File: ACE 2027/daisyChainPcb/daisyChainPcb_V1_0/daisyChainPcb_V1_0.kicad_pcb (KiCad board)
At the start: 2 copper layers, 56.5 x 97 mm, 26 parts, among them J201 Pads, J202 XT30, J203 XT30, J204 Pads, J205 Pads, J206 RJ45, J207 RJ45, U101 AP7361C-33E-13

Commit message: Ready for PCB PR
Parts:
- moved TP201 60.9 mm to (162.9, 95.8)
- moved TP203 57.1 mm to (158.9, 95.8)
- moved TP205 51.0 mm to (152.8, 78.6)
- moved TP208 45.9 mm to (141.7, 46.8)
- moved TP206 42.9 mm to (163.0, 113.4)
- moved TP207 40.4 mm to (153.0, 84.0)
- moved TP211 35.5 mm to (157.8, 61.3)
- moved TP202 31.0 mm to (152.8, 73.1)
- moved TP204 28.7 mm to (147.5, 73.0)
- moved TP209 27.6 mm to (141.2, 117.6)
- moved TP210 11.3 mm to (135.8, 115.9)
- moved R202 2.57 mm to (151.0, 63.2)
- moved R201 2.57 mm to (153.0, 63.2)
- moved J201 1.16 mm to (162.2, 81.3)
- moved J205 1.16 mm to (156.3, 86.9)
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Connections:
- J201 pad 2: /Controle/48V -> +48V
- J202 pad 2: /Controle/48V -> +48V
- J203 pad 2: /Controle/48V -> +48V
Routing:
- net +48V: track 0.00 -> 98.9 mm, vias 0 -> 1
- net /Controle/SCL: track 0.00 -> 92.4 mm, vias 0 -> 1
- net /Controle/SDA: track 0.00 -> 92.1 mm, vias 0 -> 1
- net +5V: track 0.00 -> 85.0 mm, vias 0 -> 3
- net /Controle/TX: track 0.00 -> 80.7 mm, vias 0 -> 3
- net /Controle/CAN_N: track 0.00 -> 80.4 mm, vias 0 -> 1
- net /Controle/CAN_P: track 0.00 -> 80.4 mm, vias 0 -> 1
- net /Controle/RX: track 0.00 -> 79.6 mm, vias 0 -> 3
- net VCC_3V3: track 0.00 -> 10.8 mm
- net power_GND: track 0.00 -> 7.65 mm
- added copper zone on B.Cu, net power_GND
- added copper zone on F.Cu, net signal_GND
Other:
- board text added: "3.3V"
- board text added: "5V"
- board text added: "SCL"
- board text added: "SDA"
- board text added: "Signal GND"

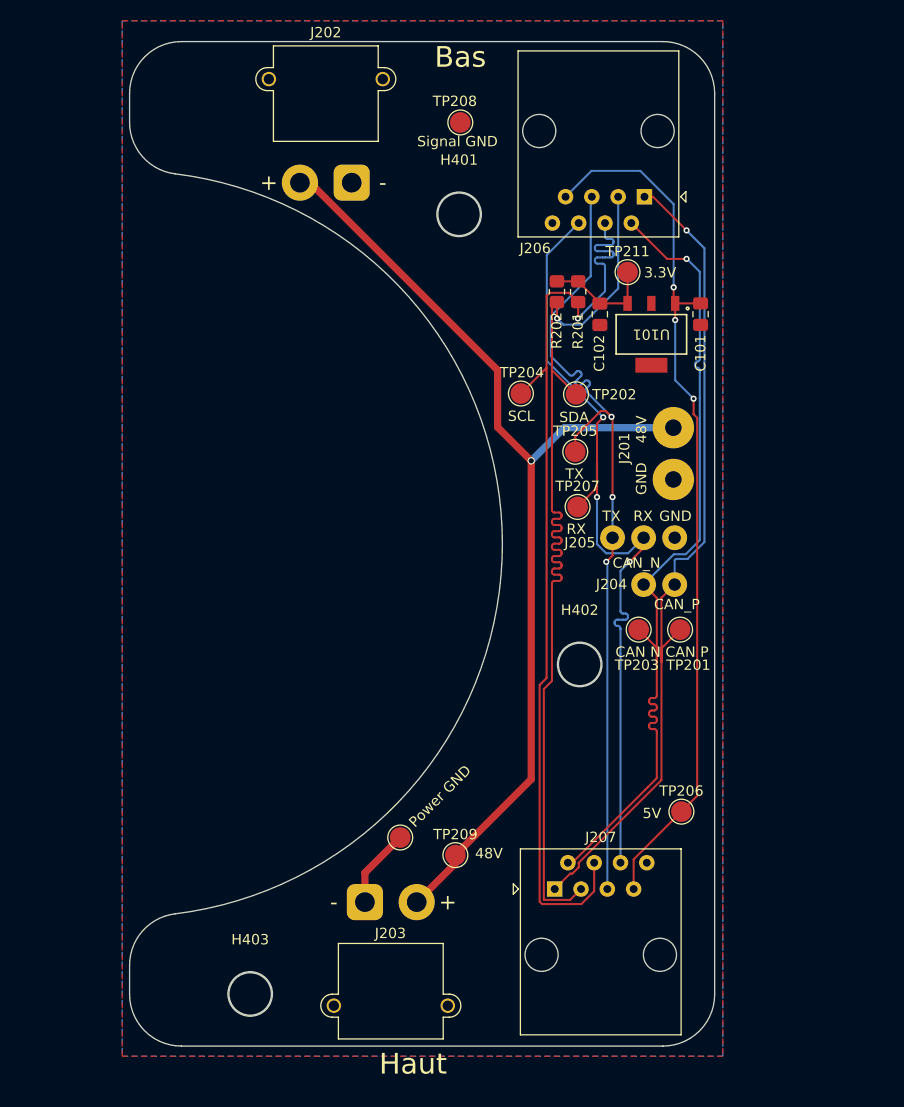
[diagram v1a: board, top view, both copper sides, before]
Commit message: amélioration de la forme du pcb
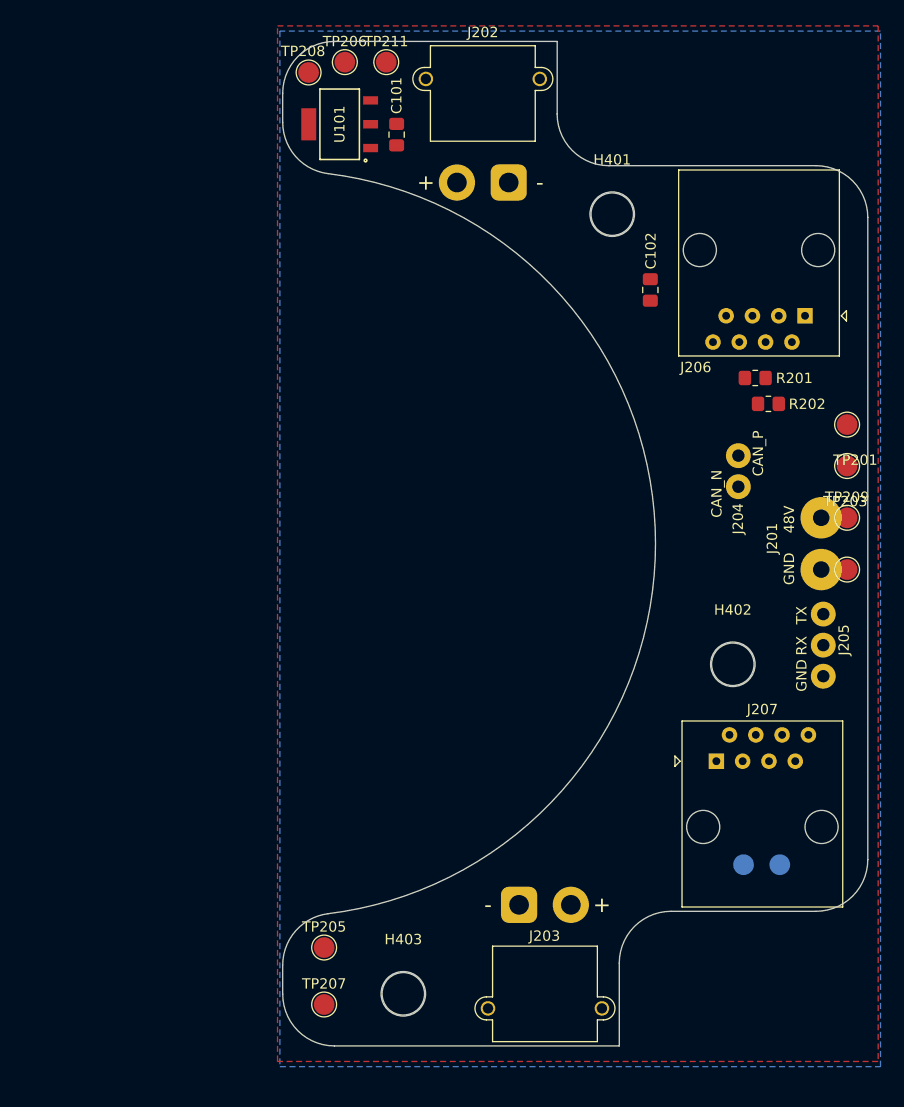
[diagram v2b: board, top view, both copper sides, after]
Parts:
- TP202, TP204: moved to B.Cu
- moved TP206 79.3 mm to (130.5, 41.0)
- moved TP207 53.9 mm to (128.5, 132.0)
- moved TP205 53.7 mm to (128.5, 126.5)
- moved TP204 51.9 mm to (172.5, 118.5), turned to 180 degrees
- moved TP210 50.3 mm to (179.0, 90.0)
- moved TP209 49.9 mm to (179.0, 85.0)
- moved TP202 48.2 mm to (169.0, 118.5), turned to 180 degrees
- moved U101 36.3 mm to (130.0, 47.0), turned to 90 degrees
- moved C101 34.1 mm to (135.5, 48.0), turned to 90 degrees
- moved TP211 30.9 mm to (134.5, 41.0)
- moved TP203 25.6 mm to (179.0, 80.0)
- moved TP201 25.5 mm to (179.0, 76.0)
- moved J205 24.4 mm to (176.7, 100.3), turned to 90 degrees
- moved R202 23.1 mm to (171.4, 74.0), turned to 180 degrees
- moved J207 19.9 mm to (166.4, 108.5)
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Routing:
- net +48V: track 98.9 -> 0.00 mm, vias 1 -> 0
- net /Controle/SCL: track 92.4 -> 0.00 mm, vias 1 -> 0
- net /Controle/SDA: track 92.1 -> 0.00 mm, vias 1 -> 0
- net +5V: track 85.0 -> 0.00 mm, vias 3 -> 0
- net /Controle/TX: track 80.7 -> 0.00 mm, vias 3 -> 0
- net /Controle/CAN_N: track 80.4 -> 0.00 mm, vias 1 -> 0
- net /Controle/CAN_P: track 80.4 -> 0.00 mm, vias 1 -> 0
- net /Controle/RX: track 79.6 -> 0.00 mm, vias 3 -> 0
- net VCC_3V3: track 10.8 -> 0.00 mm
- net power_GND: track 7.65 -> 0.00 mm
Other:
- outline, holes or cut-outs redrawn
- board text removed: "3.3V"
- board text removed: "48V"
- board text removed: "5V"
- board text removed: "Bas"
- board text removed: "CAN N"
- board text removed: "CAN P"
- board text removed: "Haut"
- board text removed: "Power GND"
- board text removed: "RX"
- board text removed: "SCL"
- board text removed: "SDA"
- board text removed: "Signal GND"
- board text removed: "TX"

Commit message: Version optimisé du PCB
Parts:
- TP201, TP203, TP205, TP207: moved to B.Cu
- TP202, TP204: moved to F.Cu
- moved TP207 45.1 mm to (172.0, 120.0), turned to 180 degrees
- moved TP204 44.8 mm to (128.5, 127.0), turned to 0 degrees
- moved TP202 43.2 mm to (128.0, 132.0), turned to 0 degrees
- moved TP205 39.0 mm to (167.0, 120.0), turned to 180 degrees
- moved TP203 26.7 mm to (173.0, 54.0), turned to 180 degrees
- moved TP201 22.1 mm to (177.5, 54.0), turned to 180 degrees
- moved J207 4.00 mm to (162.4, 108.5)
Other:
- outline, holes or cut-outs redrawn

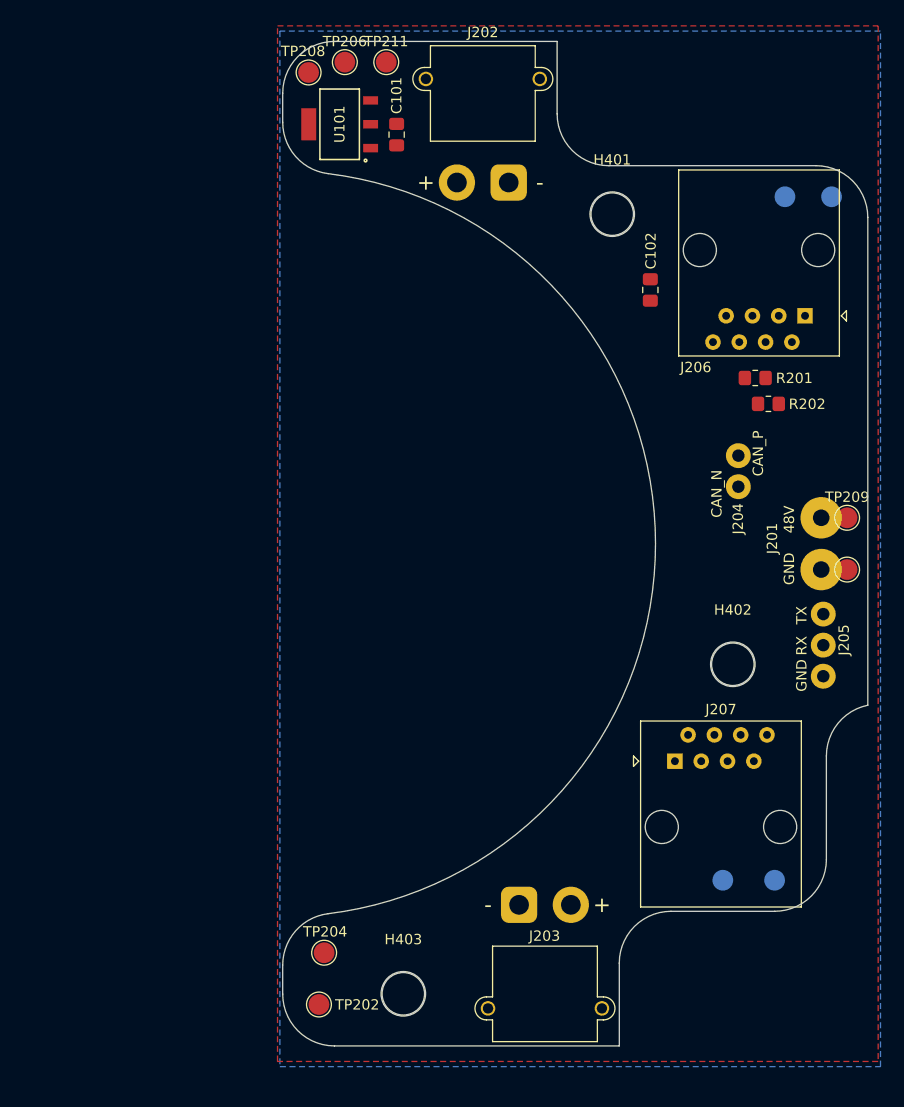
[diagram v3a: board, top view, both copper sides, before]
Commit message: deplacement petit capaciteur
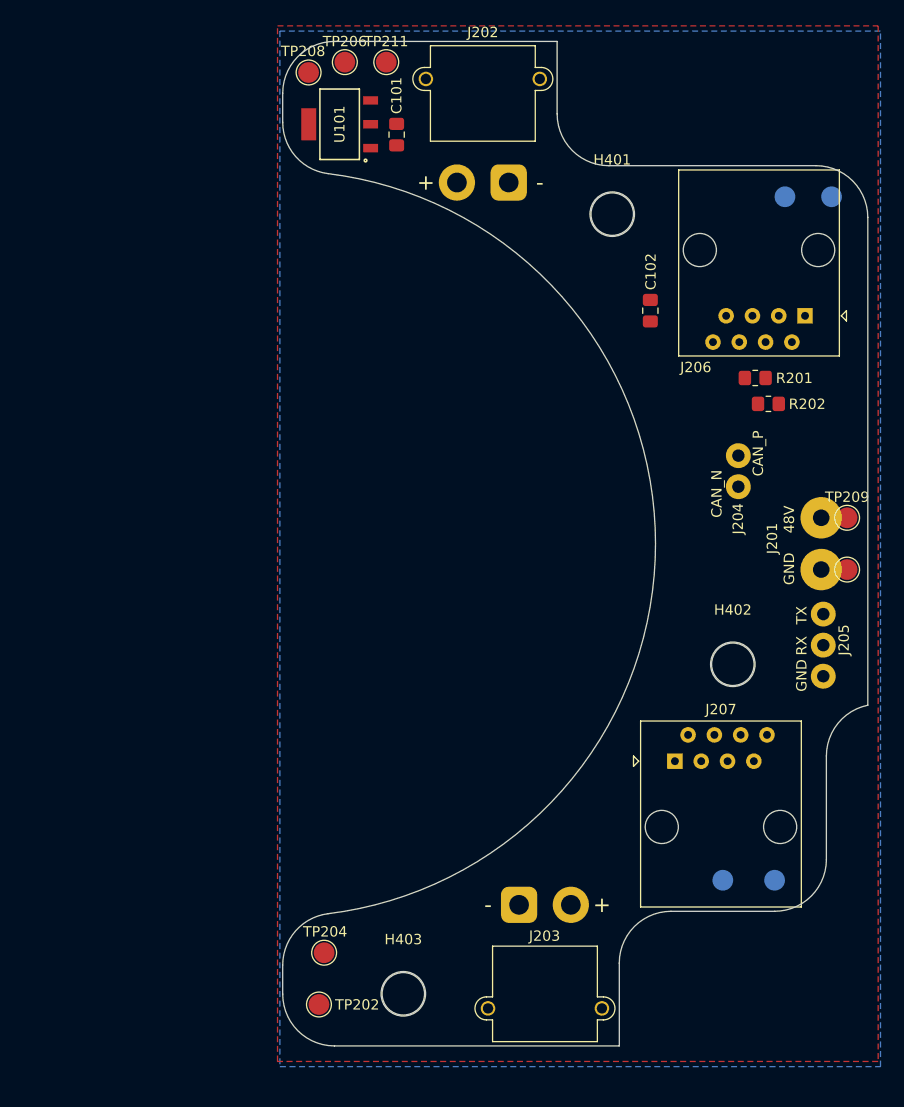
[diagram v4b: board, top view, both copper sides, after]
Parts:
- moved C102 2.00 mm to (160.0, 65.0)
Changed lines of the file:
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@@
 	(footprint "Capacitor_SMD:C_0805_2012Metric_Pad1.18x1.45mm_HandSolder"
 		(layer "F.Cu")
-		(at 160 63 90)
+		(at 160 65 90)
 		(descr "Capacitor SMD 0805 (2012 Metric), square (rectangular) end terminal, IPC-7351 nominal with elongated pad for handsoldering. (Body size source: IPC-SM-782 page 76, https://www.pcb-3d.com/wordpress/wp-content/uploads/ipc-sm-782a_amendment_1_and_2.pdf, https://docs.google.com/spreadsheets/d/1BsfQQcO9C6DZCsRaXUlFlo91Tg2WpOkGARC1WS5S8t0/edit?usp=sharing)")
 		(tags "capacitor handsolder")
@@
 		(end 124.5 46.80602)
 		(stroke
-			(width 0)
+			(width 0.1)
 			(type default)
 		)
@@
 		(end 129.5 39)
 		(stroke
-			(width 0)
+			(width 0.1)
 			(type default)
 		)
@@
 		(end 124.5 131)
 		(stroke
-			(width 0)
+			(width 0.1)
 			(type default)
 		)
@@
 		(end 128.890244 123.231299)
 		(stroke
-			(width 0)
+			(width 0.1)
 			(type default)
 		)
@@
 		(end 124.5 46.80602)
 		(stroke
-			(width 0)
+			(width 0.1)
 			(type default)
 		)
@@
 		(end 128.890244 123.231299)
 		(stroke
-			(width 0)
+			(width 0.1)
 			(type default)
 		)
@@
 		(end 124.5 131)
 		(stroke
-			(width 0)
+			(width 0.1)
 			(type default)
 		)
@@
 		(end 157 136)
 		(stroke
-			(width 0)
+			(width 0.1)
 			(type default)
 		)
@@
 		(end 138.196857 130.966662)
 		(stroke
-			(width 0)
+			(width 0.1)
 			(type default)
 		)
@@
 		(end 129.5 39)
 		(stroke
-			(width 0)
+			(width 0.1)
 			(type default)
 		)
@@
 		(end 151 46)
 		(stroke
-			(width 0)
+			(width 0.1)
 			(type default)
 		)
@@
 		(end 151 46)
 		(stroke
-			(width 0)
+			(width 0.1)
 			(type default)
 		)
@@
 		(end 176 51)
 		(stroke
-			(width 0)
+			(width 0.1)
 			(type default)
 		)
@@
 		(end 158.369805 55.680195)
 		(stroke
-			(width 0)
+			(width 0.1)
 			(type default)
 		)
@@
 		(end 157 136)
 		(stroke
-			(width 0)
+			(width 0.1)
 			(type default)
 		)
@@
 		(end 162 123)
 		(stroke
-			(width 0)
+			(width 0.1)
 			(type default)
 		)
@@
 		(end 170.016662 99.146857)
 		(stroke
-			(width 0)
+			(width 0.1)
 			(type default)
 		)
@@
 		(end 162 123)
 		(stroke
-			(width 0)
+			(width 0.1)
 			(type default)
 		)
@@
 		(end 181 56)
 		(stroke
-			(width 0)
+			(width 0.1)
 			(type default)
 		)
@@
 		(end 181 103.101021)
 		(stroke
-			(width 0)
+			(width 0.1)
 			(type default)
 		)
@@
 		(end 172 123)
 		(stroke
-			(width 0)
+			(width 0.1)
 			(type default)
 		)
@@
 		(end 177 108)
 		(stroke
-			(width 0)
+			(width 0.1)
 			(type default)
 		)
@@
 		(end 181 56)
 		(stroke
-			(width 0)
-			(type default)
-		)
+			(width 0.1)
+			(type default)
+		)
